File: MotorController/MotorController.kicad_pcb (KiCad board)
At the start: 2 copper layers, 55 x 45 mm, 44 parts, among them J1 4P4C, J2 AVR-ISP-10, J3 8P8C, J4 Screw_Terminal_01x02, Q1 Q_NMOS_GSD, SW2 SW_Push, U1 LD1117S50TR_SOT223, U2 MAX485E, U3 ATmega8A-AU, Y1 8Mhz

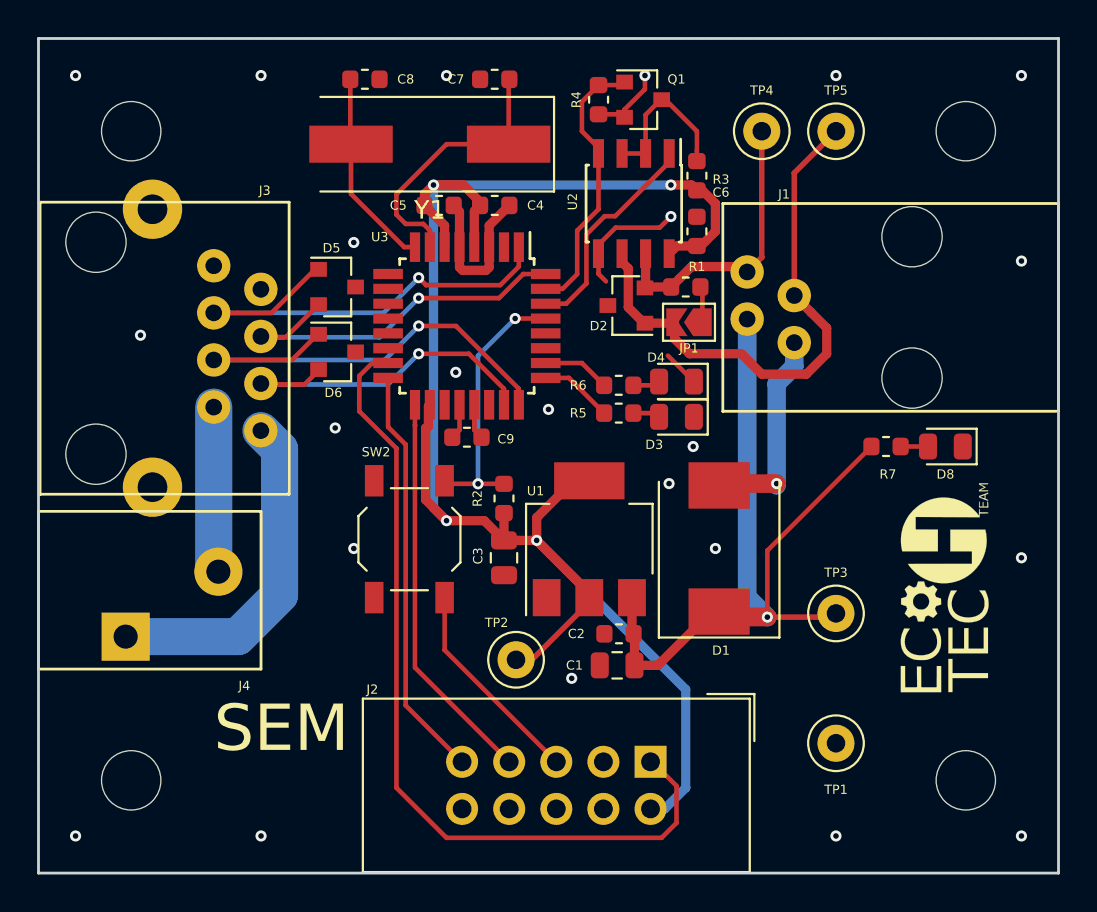
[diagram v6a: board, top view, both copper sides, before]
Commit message: Changed all via diameters to 0.7. Added project and version label on silk screen. Added more grounding vias.
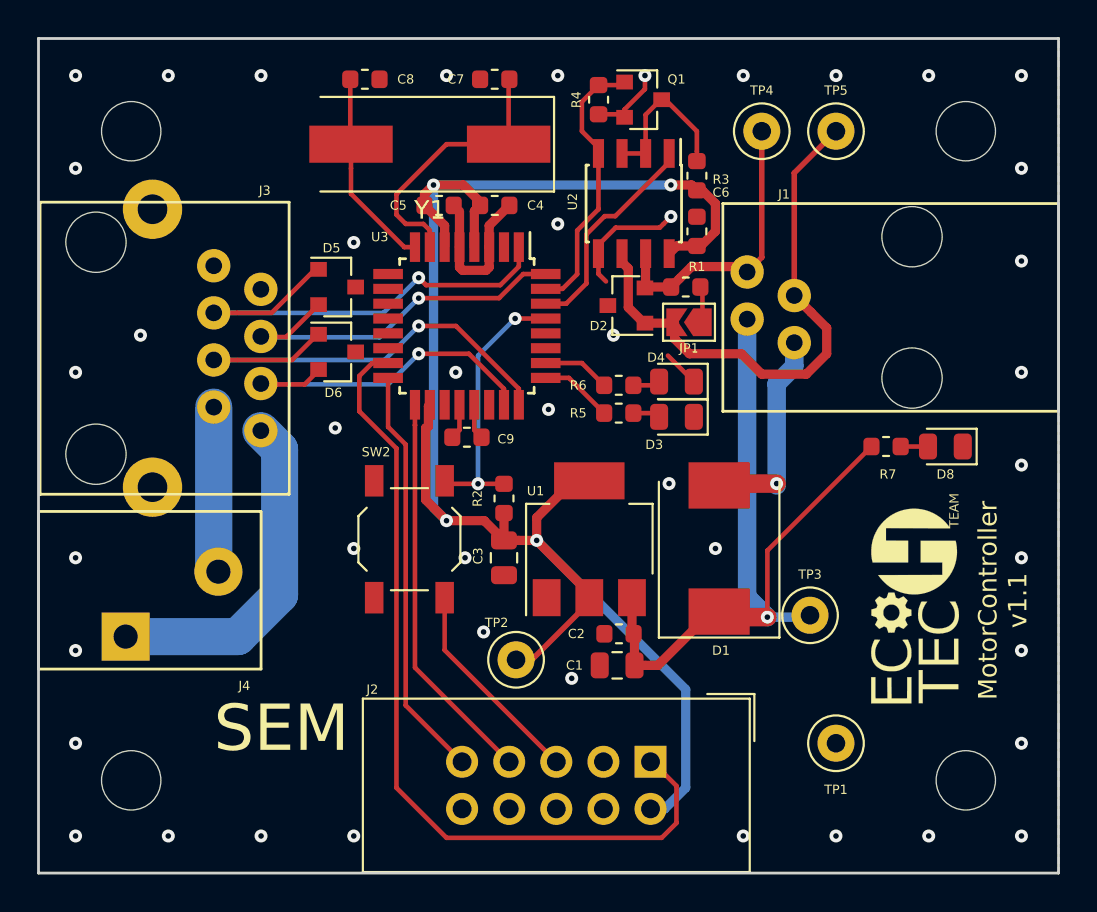
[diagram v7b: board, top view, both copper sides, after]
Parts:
- moved G1 1.71 mm to (122.5, 90.5)
- moved TP3 1.40 mm to (116.6, 91.1)
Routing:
- net +12V: track 44.1 -> 43.3 mm
- net GND: vias 24 -> 45
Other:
- net class Default: via_dia 0.6 -> 0.7
- net class Power: via_dia 0.6 -> 0.7
- net class Wide: via_dia 0.6 -> 0.7
- rule via_min_size: 0.4 -> 0.7
- board text added: "MotorController v1.1"

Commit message: Changed 1.1 to 1.0 versions.
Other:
- board text added: "MotorController v1.0"
- board text removed: "MotorController v1.1"
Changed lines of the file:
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@@
     )
   )
-  (gr_text "MotorController\nv1.1" (at 127 90.3 90) (layer F.SilkS)
+  (gr_text "MotorController\nv1.0\n" (at 127 90.3 90) (layer F.SilkS)
     (effects (font (size 1 1) (thickness 0.2)))
   )
